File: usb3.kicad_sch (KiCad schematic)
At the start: 50 parts, among them J5 632723300011, Q13 PJE138K, Q4 PJE138K, U17 HD3SS3220RNH, U18 AP22615A, U19 TPD4E05U06QDQARQ1, U20 TPD4E05U06QDQARQ1, U21 TPD4E05U06QDQARQ1

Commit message: Initial layout attempt
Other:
- note added: "Simplify to USBA"

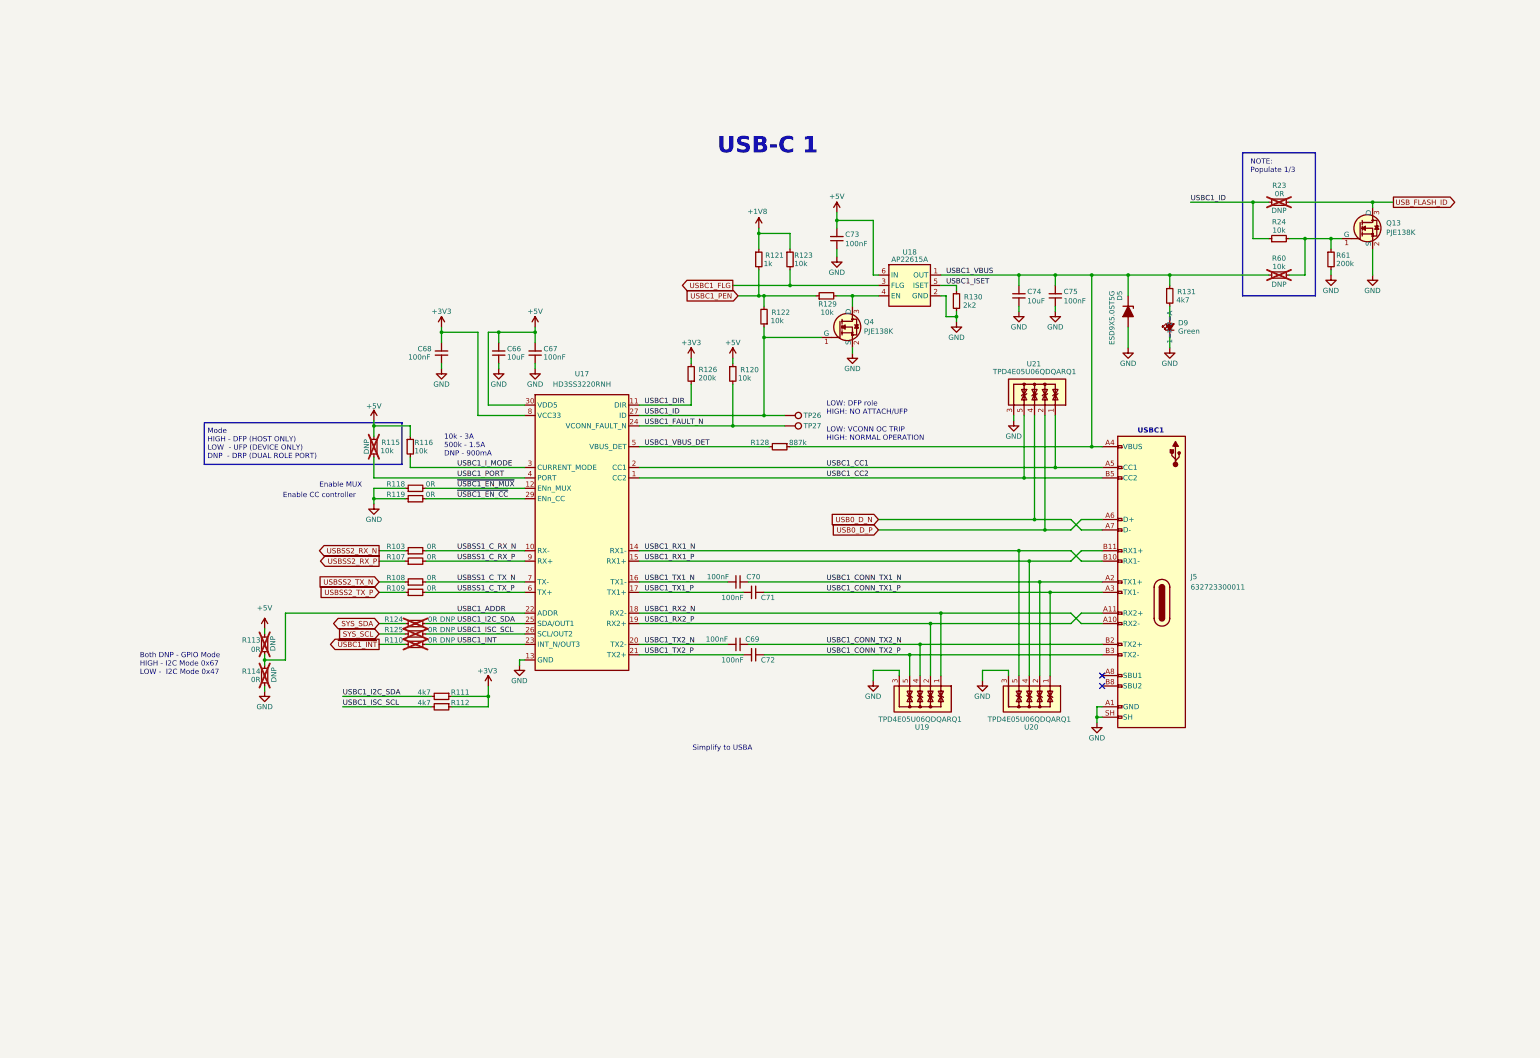
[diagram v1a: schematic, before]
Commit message: Finish HDMI routing, replace usbc w/ usba
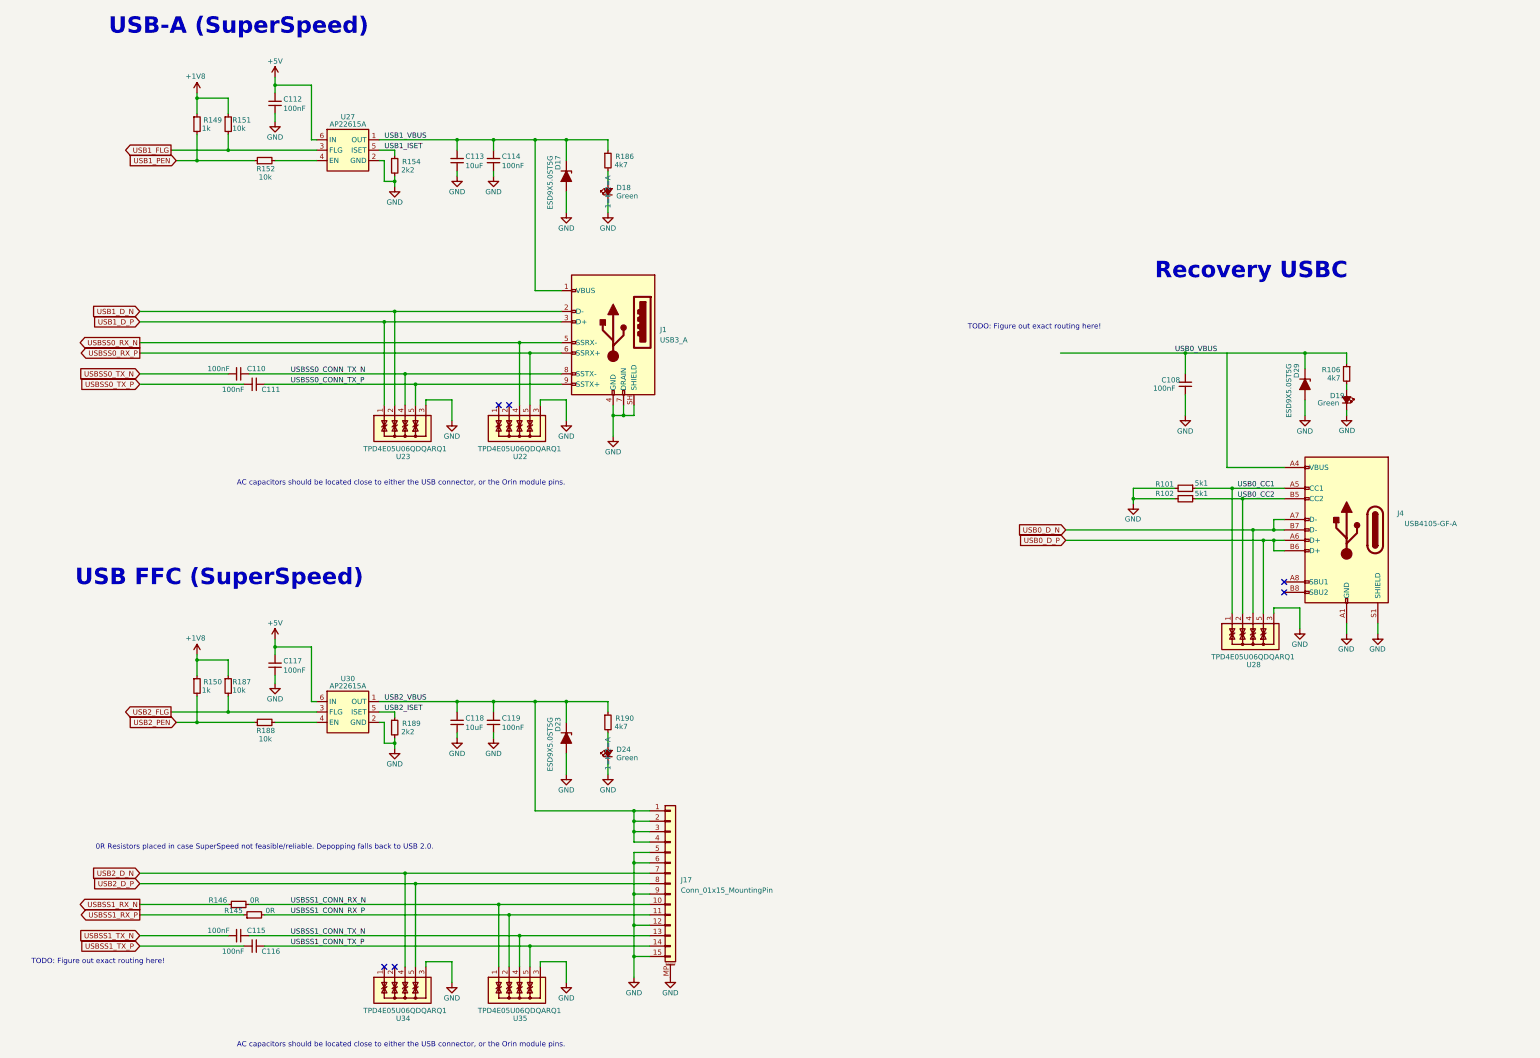
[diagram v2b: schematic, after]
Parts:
- removed C66: 10uF, Capacitor_SMD:C_0402_1005Metric, symbol Device:C_Small
- removed C67, C68, C69, C70, C71, C72: 100nF, Capacitor_SMD:C_0402_1005Metric, symbol Device:C_Small
- removed C73, C75: 100nF, Capacitor_SMD:C_0603_1608Metric, symbol Device:C_Small
- removed C74: 10uF, Capacitor_SMD:C_0603_1608Metric, symbol Device:C_Small
- removed D5: ESD9X5.0ST5G, Diode_SMD:D_SOD-923, symbol Device:D_Zener_Filled
- removed D9: LED_G_0603_LTST-C190GKT, LED_SMD:LED_0603_1608Metric, symbol Device:LED_Small_Filled
- removed J5: 632723300011, JetsonCarrier:USB-C_Receptacle_WE_632723300011, symbol JetsonCarrier:USB-C_WE_632723300011
- removed Q13, Q4: PJE138K, Package_TO_SOT_SMD:SOT-523, symbol JetsonCarrier:PJE138K
- removed R103, R107, R108, R109, R110, R113, R114, R118, R119, R124, R125: 0R, Resistor_SMD:R_0402_1005Metric, symbol Device:R_Small
- removed R111, R112, R131: 4k7, Resistor_SMD:R_0402_1005Metric, symbol Device:R_Small
- removed R115, R116, R120, R122, R123, R129: 10k, Resistor_SMD:R_0402_1005Metric, symbol Device:R_Small
- removed R121: 1k, Resistor_SMD:R_0402_1005Metric, symbol Device:R_Small
- removed R126: 200k, Resistor_SMD:R_0402_1005Metric, symbol Device:R_Small
- removed R128: 887k, Resistor_SMD:R_0402_1005Metric, symbol Device:R_Small
- removed R130: 2k2, Resistor_SMD:R_0402_1005Metric, symbol Device:R_Small
- removed R23: 0R, Resistor_SMD:R_0603_1608Metric, symbol Device:R_Small
- removed R24, R60: 10k, Resistor_SMD:R_0603_1608Metric, symbol Device:R_Small
- removed R61: 200k, Resistor_SMD:R_0603_1608Metric, symbol Device:R_Small
- removed TP26, TP27: TP_0.75mm_SMD, JetsonCarrier:TP_SMD_0.75mm, symbol Connector:TestPoint
- removed U17: HD3SS3220RNH, JetsonCarrier:WQFN-30-1EP_4.6x2.6mm_P0.4mm, symbol JetsonCarrier:HD3SS3220RNH
- removed U18: AP22615A, Package_TO_SOT_SMD:TSOT-23-6, symbol JetsonCarrier:AP22615A_TSOT26
- removed U19, U20, U21: TPD4E05U06QDQARQ1, JetsonCarrier:USON-10_2.5x1mm_P0.5mm, symbol JetsonCarrier:TPD4E05U06QDQARQ1
- added C108, C112, C114, C117, C119: 100nF, Capacitor_SMD:C_0603_1608Metric, symbol Device:C_Small
- added C110, C111, C115, C116: 100nF, Capacitor_SMD:C_0402_1005Metric, symbol Device:C_Small
- added C113, C118: 10uF, Capacitor_SMD:C_0603_1608Metric, symbol Device:C_Small
- added D17, D23, D29: ESD9X5.0ST5G, Diode_SMD:D_SOD-923, symbol Device:D_Zener_Filled
- added D18, D19, D24: LED_G_0603_LTST-C190GKT, LED_SMD:LED_0603_1608Metric, symbol Device:LED_Small_Filled
- added J1: USB3_A, Connector_USB:USB3_A_Molex_48393-001, symbol Connector:USB3_A
- added J17: Conn_01x15_MountingPin, Connector_FFC-FPC:Amphenol_F32Q-1A7x1-11015_1x15-1MP_P0.5mm_Horizontal, symbol Connector_Generic_MountingPin:Conn_01x15_MountingPin
- added J4: USB4105-GF-A, Connector_USB:USB_C_Receptacle_GCT_USB4105-xx-A_16P_TopMnt_Horizontal, symbol Connector:USB_C_Receptacle_USB2.0_16P
- added R101, R102: 5k1, Resistor_SMD:R_0402_1005Metric, symbol Device:R_Small
- added R106: 4k7, Resistor_SMD:R_0603_1608Metric, symbol Device:R_Small
- added R145, R146: 0R, Resistor_SMD:R_0402_1005Metric, symbol Device:R_Small
- added R149, R150: 1k, Resistor_SMD:R_0402_1005Metric, symbol Device:R_Small
- added R151, R152, R187, R188: 10k, Resistor_SMD:R_0402_1005Metric, symbol Device:R_Small
- added R154, R189: 2k2, Resistor_SMD:R_0402_1005Metric, symbol Device:R_Small
- added R186, R190: 4k7, Resistor_SMD:R_0402_1005Metric, symbol Device:R_Small
- added U22, U23, U28, U34, U35: TPD4E05U06QDQARQ1, Argus-Miscellaneous:USON-10_TEX, symbol JetsonCarrier:TPD4E05U06QDQARQ1
- added U27, U30: AP22615A, Package_TO_SOT_SMD:TSOT-23-6, symbol JetsonCarrier:AP22615A_TSOT26
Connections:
- net +1V8: now also R149.1, R150.1, R151.1, R187.1
- net +5V: now also C112.2, C117.2, U27.6 (IN), U30.6 (IN)
- net GND: now also C108.1, C112.1, C113.1, C114.1, C117.1, C118.1, C119.1, D17.2 (A), D18.1 (K), D19.1 (K), D23.2 (A), D24.1 (K), D29.2 (A), J1.4 (GND), J1.7 (DRAIN), J1.SH (SHIELD), J17.12 (Pin_12), J17.15 (Pin_15), J17.5 (Pin_5), J17.6 (Pin_6), J17.9 (Pin_9), J17.MP (MountPin), J4.A1 (GND), J4.A12 (GND), J4.B1 (GND), J4.B12 (GND), J4.S1 (SHIELD), R101.2, R102.2, R154.2, R189.2, U22.3, U22.8, U23.3, U23.8, U27.2 (GND), U28.3, U28.8, U30.2 (GND), U34.3, U34.8, U35.3, U35.8
- net USB0_D_N: now also J4.A7 (D-), J4.B7 (D-), U28.4, U28.7
- net USB0_D_P: now also J4.A6 (D+), J4.B6 (D+), U28.5, U28.6
- new net: D24.2 (A), R190.2
- new net: R152.2, U27.4 (EN)
- new net: U22.1, U22.10
- new net: U22.2, U22.9
- new net: D19.2 (A), R106.2
- new net: R188.2, U30.4 (EN)
- new net: J4.A4 (VBUS), J4.A9 (VBUS), J4.B4 (VBUS), J4.B9 (VBUS)
- new net: U34.1, U34.10
- new net: U34.2, U34.9
- new net: D18.2 (A), R186.2
- new net USB0_CC1: J4.A5 (CC1), R101.1, U28.1, U28.10
- new net USB0_CC2: J4.B5 (CC2), R102.1, U28.2, U28.9
- new net USB0_VBUS: C108.2, D29.1 (K), R106.1
- new net USB1_D_N: J1.2 (D-), U23.2, U23.9
- new net USB1_D_P: J1.3 (D+), U23.1, U23.10
- new net USB1_FLG: R151.2, U27.3 (FLG)
- new net USB1_ISET: R154.1, U27.5 (ISET)
- new net USB1_PEN: R149.2, R152.1
- new net USB1_VBUS: C113.2, C114.2, D17.1 (K), J1.1 (VBUS), R186.1, U27.1 (OUT)
- new net USB2_D_N: J17.7 (Pin_7), U34.4, U34.7
- new net USB2_D_P: J17.8 (Pin_8), U34.5, U34.6
- new net USB2_FLG: R187.2, U30.3 (FLG)
- new net USB2_ISET: R189.1, U30.5 (ISET)
- new net USB2_PEN: R150.2, R188.1
- new net USB2_VBUS: C118.2, C119.2, D23.1 (K), J17.1 (Pin_1), J17.2 (Pin_2), J17.3 (Pin_3), J17.4 (Pin_4), R190.1, U30.1 (OUT)
- new net USBSS0_CONN_TX_N: C110.1, J1.8 (SSTX-), U23.4, U23.7
- new net USBSS0_CONN_TX_P: C111.1, J1.9 (SSTX+), U23.5, U23.6
- new net USBSS0_RX_N: J1.5 (SSRX-), U22.4, U22.7
- new net USBSS0_RX_P: J1.6 (SSRX+), U22.5, U22.6
- new net USBSS0_TX_N: C110.2
- new net USBSS0_TX_P: C111.2
- new net USBSS1_CONN_RX_N: J17.10 (Pin_10), R146.2, U35.1, U35.10
- new net USBSS1_CONN_RX_P: J17.11 (Pin_11), R145.2, U35.2, U35.9
- new net USBSS1_CONN_TX_N: C115.1, J17.13 (Pin_13), U35.4, U35.7
- new net USBSS1_CONN_TX_P: C116.1, J17.14 (Pin_14), U35.5, U35.6
- new net USBSS1_RX_N: R146.1
- new net USBSS1_RX_P: R145.1
- new net USBSS1_TX_N: C115.2
- new net USBSS1_TX_P: C116.2
- no-connect marks 2 -> 6
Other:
- note added: "0R Resistors placed in case SuperSpeed not feasible/reliable. Depopping falls back to USB 2.0."
- note added: "AC capacitors should be located close to either the USB connector, or the Orin module pins."
- note added: "Recovery USBC"
- note added: "TODO: Figure out exact routing here!"
- note added: "USB FFC (SuperSpeed)"
- note added: "USB-A (SuperSpeed)"
- note removed: "10k - 3A 500k - 1.5A DNP - 900mA"
- note removed: "Both DNP - GPIO Mode HIGH - I2C Mode 0x67 LOW - I2C Mode 0x47"
- note removed: "Enable CC controller"
- note removed: "Enable MUX"
- note removed: "LOW: DFP role HIGH: NO ATTACH/UFP"
- note removed: "LOW: VCONN OC TRIP HIGH: NORMAL OPERATION"
- note removed: "Mode HIGH - DFP (HOST ONLY) LOW - UFP (DEVICE ONLY) DNP - DRP (DUAL ROLE PORT)"
- note removed: "NOTE: Populate 1/3"
- note removed: "Simplify to USBA"
- note removed: "USB-C 1"
- note removed: "USBC1"

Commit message: Add CSI, USB, HDMI, PCIe
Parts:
- R186: footprint Resistor_SMD:R_0402_1005Metric -> Resistor_SMD:R_0603_1608Metric

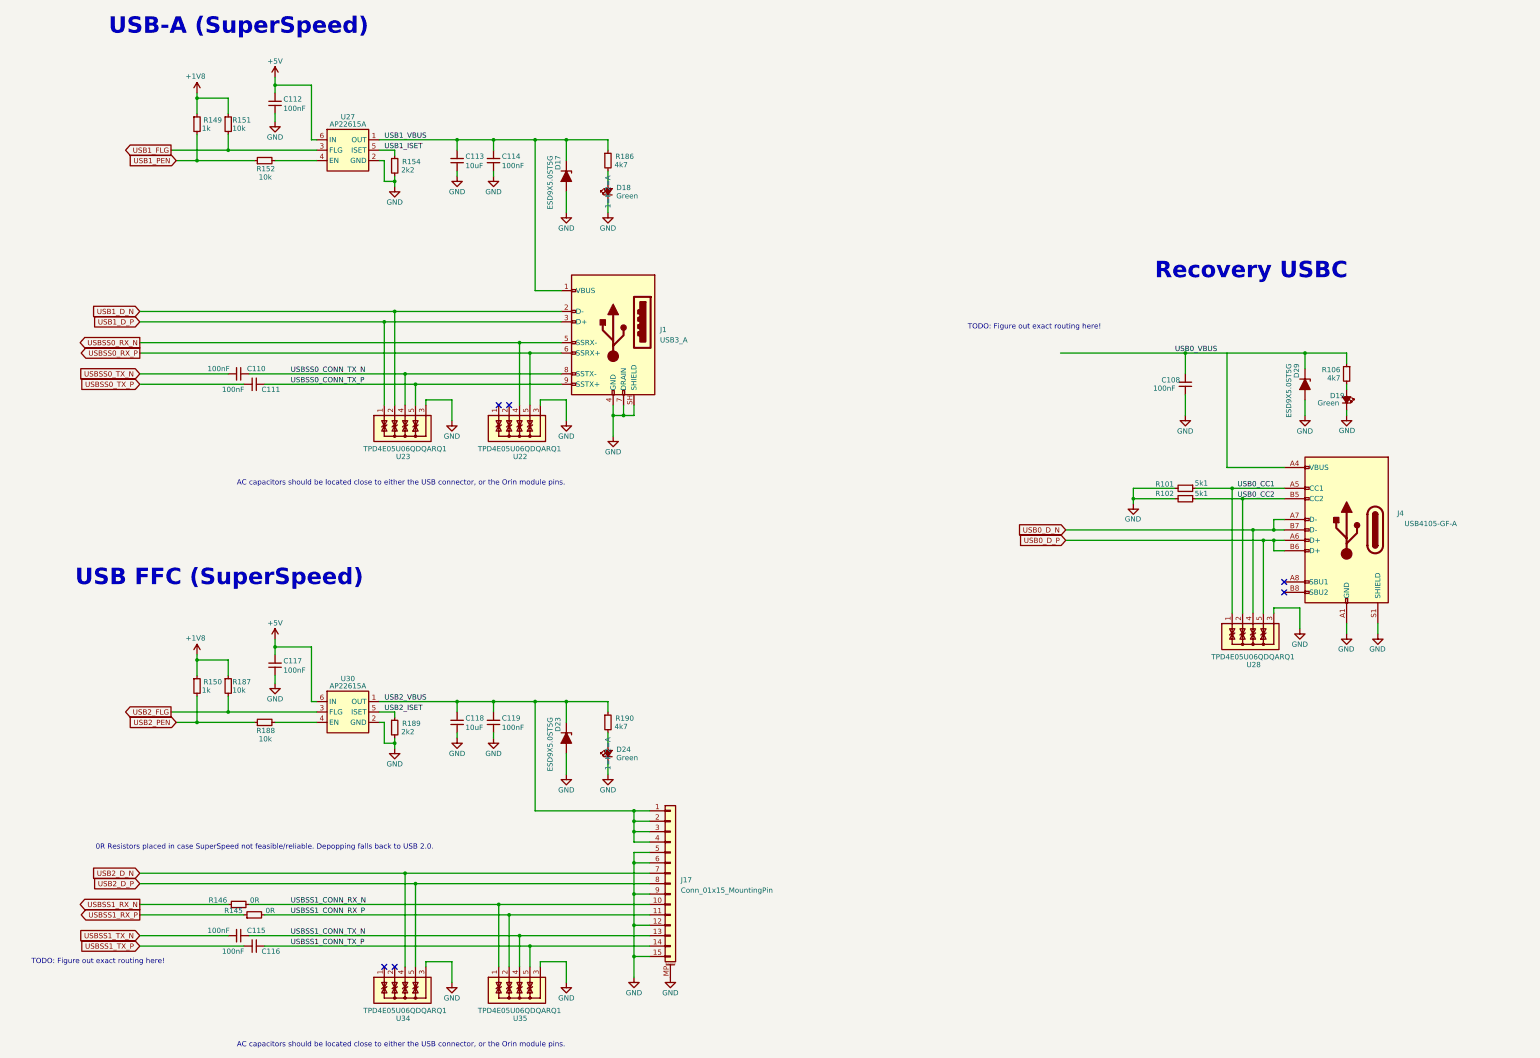
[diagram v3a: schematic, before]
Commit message: Power routing, CSI length matching, cleanup
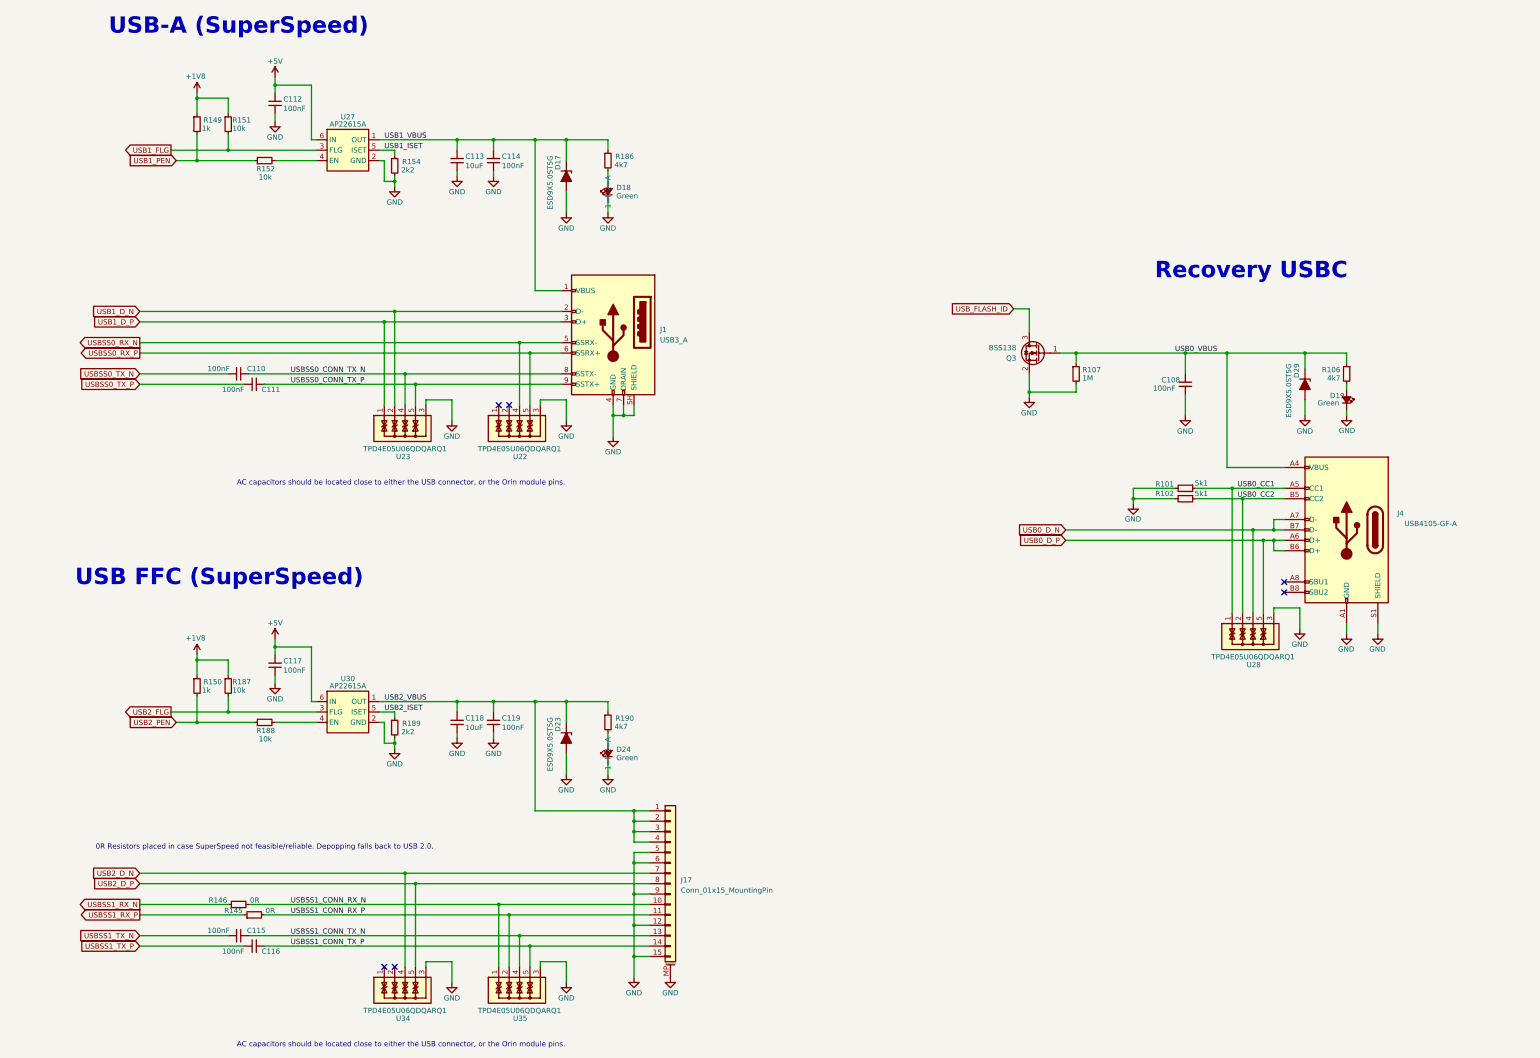
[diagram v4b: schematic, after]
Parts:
- added Q3: BSS138, Package_TO_SOT_SMD:SOT-23, symbol Transistor_FET:BSS138
- added R107: 1M, Resistor_SMD:R_0603_1608Metric, symbol Device:R_Small
- R149, R150, R151, R152, R154, R187, R188, R189, R190: footprint Resistor_SMD:R_0402_1005Metric -> Resistor_SMD:R_0603_1608Metric
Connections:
- net GND: now also Q3.2 (S), R107.2
- net USB0_VBUS: now also J4.A4 (VBUS), J4.A9 (VBUS), J4.B4 (VBUS), J4.B9 (VBUS), Q3.1 (G), R107.1
- new net USB_FLASH_ID: Q3.3 (D)
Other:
- note removed: "TODO: Figure out exact routing here!"
